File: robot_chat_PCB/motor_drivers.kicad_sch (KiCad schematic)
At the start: 22 parts, among them IC401 NCS199A3RSQT2G, IC402 NCS199A3RSQT2G, J401 Conn_01x06, J402 Conn_01x06, U401 ZXBM5210-SP-13, U402 ZXBM5210-SP-13

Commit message: Mise à jour placement
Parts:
- removed U401, U402: ZXBM5210-SP-13, Package_SO:SOIC-8-1EP_3.9x4.9mm_P1.27mm_EP2.62x3.51mm_ThermalVias, symbol Driver_Motor:ZXBM5210-S
- added U401, U402: ZXBM5210-SP, Package_SO:SOIC-8-1EP_3.9x4.9mm_P1.27mm_EP2.62x3.51mm_ThermalVias, symbol Driver_Motor:ZXBM5210-SP
- C201, C401, C404: footprint Capacitor_SMD:C_0603_1608Metric -> Capacitor_SMD:C_0402_1005Metric
- J401: value Conn_01x06 -> L_Mot
- J402: value Conn_01x06 -> R_Mot
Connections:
- net +3V3: now also U401.3 (VDD), U401.6 (VREF), U402.3 (VDD), U402.6 (VREF)
- net FWD_L: now also U402.4 (FWD)
- net FWD_R: now also U401.4 (FWD)
- net GND: now also U401.8 (GND), U401.9 (GND), U402.8 (GND), U402.9 (GND)
- net MOTOR_L+: now also J401.1 (Pin_1), U402.7 (OUT2); no longer J401.6 (Pin_6)
- net MOTOR_L-: now also J401.6 (Pin_6), U402.1 (OUT1); no longer J401.1 (Pin_1)
- net MOTOR_R+: now also J402.1 (Pin_1), U401.7 (OUT2); no longer J402.6 (Pin_6)
- net MOTOR_R-: now also J402.6 (Pin_6), U401.1 (OUT1); no longer J402.1 (Pin_1)
- net REV_L: now also U402.5 (REV)
- net REV_R: now also U401.5 (REV)
- net RSENSE_L-: now also U402.2 (VM)
- net RSENSE_R-: now also U401.2 (VM)

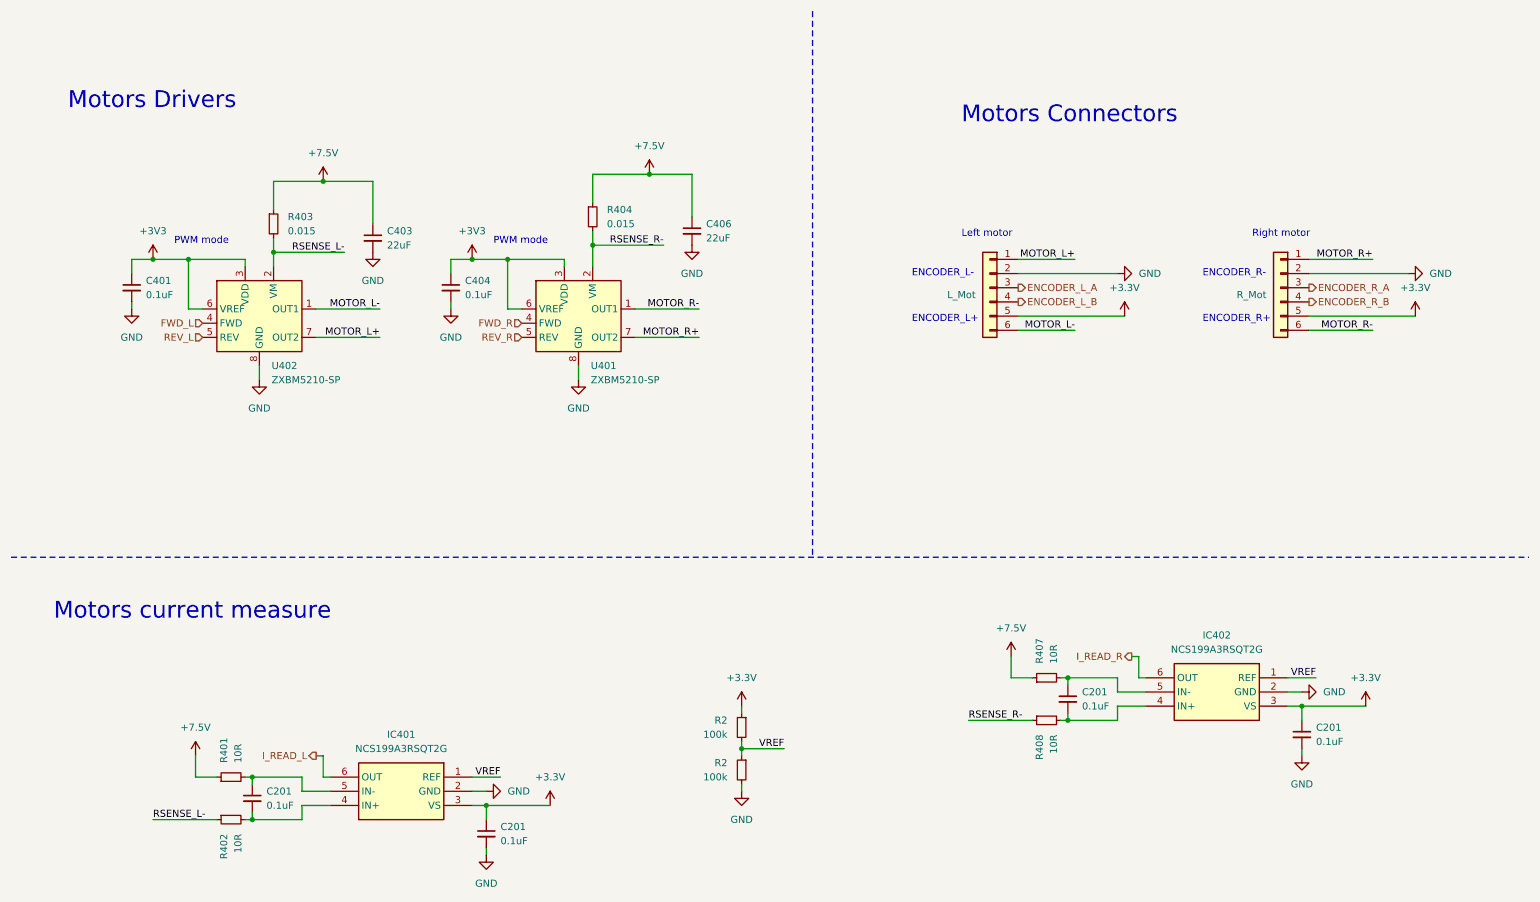
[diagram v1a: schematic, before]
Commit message: changed Rsense position
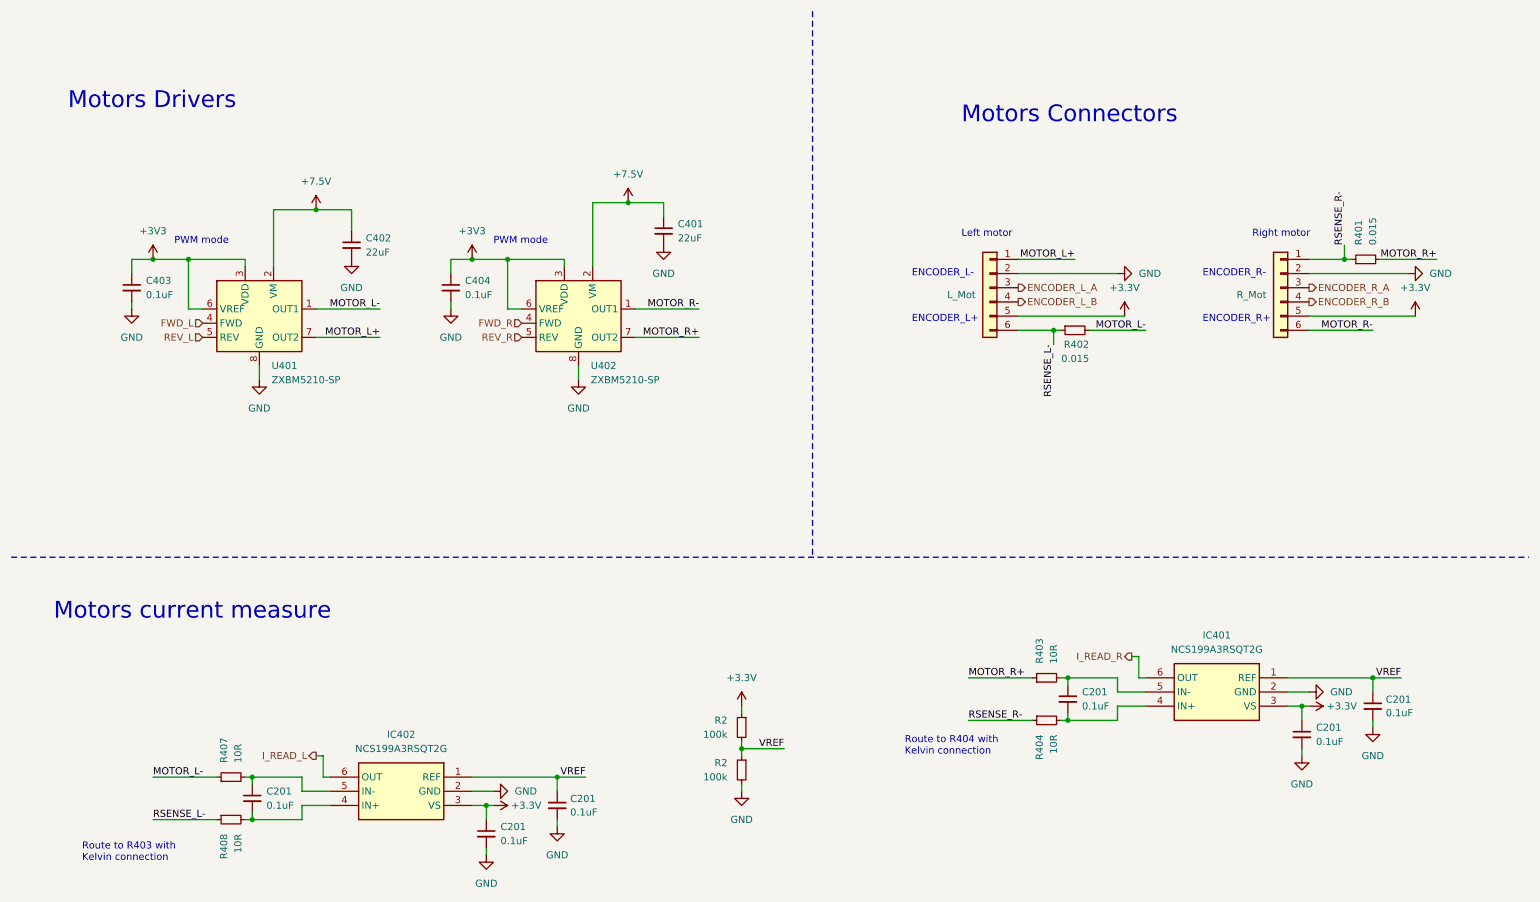
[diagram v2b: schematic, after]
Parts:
- added C201 (x2): 0.1uF, Capacitor_SMD:C_0402_1005Metric, symbol Device:C_Small
- renumbered C406 to C401, C403 to C402, C401 to C403, IC402 to IC401, IC401 to IC402, R404 to R401, R403 to R402, R407 to R403, R408 to R404, R401 to R407, R402 to R408, U402 to U401, U401 to U402
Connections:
- net +7.5V: now also U401.2 (VM), U402.2 (VM); no longer R401.1, R402.1, R403.1, R407.1
- net GND: now also C201.2, C201.2
- net MOTOR_L-: now also R402.2, R407.1; no longer J401.6 (Pin_6)
- net MOTOR_R+: now also R401.2, R403.1; no longer J402.1 (Pin_1)
- net RSENSE_L-: now also J401.6 (Pin_6), R402.1; no longer R402.2, U401.2 (VM)
- net RSENSE_R-: now also J402.1 (Pin_1), R401.1; no longer R401.2, U402.2 (VM)
- net VREF: now also C201.1, C201.1
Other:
- note added: "Route to R403 with Kelvin connection"
- note added: "Route to R404 with Kelvin connection"
- moved on the sheet: C401, C402, R401, R402

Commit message: Routage
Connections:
- net +3V3 is gone; now on net +3.3V: C403.1, C404.1, U401.3 (VDD), U401.6 (VREF), U402.3 (VDD), U402.6 (VREF)
- net MOTOR_L-: now also R408.1; no longer R407.1
- net RSENSE_L-: now also R407.1; no longer R408.1
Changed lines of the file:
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@@
   (junction (at 44.45 57.15) (diameter 0) (color 0 0 0 0)
   )
+  (junction (at 36.83 57.15) (diameter 0) (color 0 0 0 0)
+  )
   (junction (at 55.88 149.86) (diameter 0) (color 0 0 0 0)
   )
+  (junction (at 93.98 57.15) (diameter 0) (color 0 0 0 0)
+  )
   (junction (at 55.88 157.48) (diameter 0) (color 0 0 0 0)
   )
@@
   (junction (at 67.31 48.26) (diameter 0) (color 0 0 0 0)
   )
-  (junction (at 38.1 57.15) (diameter 0) (color 0 0 0 0)
-  )
   (junction (at 199.39 69.85) (diameter 0) (color 0 0 0 0)
   )
   (junction (at 201.93 139.7) (diameter 0) (color 0 0 0 0)
   )
-  (junction (at 95.25 57.15) (diameter 0) (color 0 0 0 0)
-  )
   (junction (at 101.6 57.15) (diameter 0) (color 0 0 0 0)
   )
@@
     (stroke (width 0) (type default))
   )
-  (wire (pts (xy 95.25 57.15) (xy 101.6 57.15))
+  (wire (pts (xy 91.44 57.15) (xy 93.98 57.15))
     (stroke (width 0) (type default))
   )
@@
   )
   (wire (pts (xy 91.44 59.69) (xy 91.44 57.15))
-    (stroke (width 0) (type default))
-  )
-  (wire (pts (xy 91.44 57.15) (xy 95.25 57.15))
     (stroke (width 0) (type default))
   )
@@
     (stroke (width 0) (type default))
   )
+  (wire (pts (xy 93.98 57.15) (xy 101.6 57.15))
+    (stroke (width 0) (type default))
+  )
   (wire (pts (xy 135.89 66.04) (xy 124.46 66.04))
     (stroke (width 0) (type default))
@@
     (stroke (width 0) (type default))
   )
-  (wire (pts (xy 34.29 57.15) (xy 38.1 57.15))
-    (stroke (width 0) (type default))
-  )
   (wire (pts (xy 256.54 69.85) (xy 245.11 69.85))
     (stroke (width 0) (type default))
   )
-  (wire (pts (xy 38.1 57.15) (xy 44.45 57.15))
+  (wire (pts (xy 34.29 57.15) (xy 36.83 57.15))
     (stroke (width 0) (type default))
   )
@@
   )
   (wire (pts (xy 44.45 66.04) (xy 44.45 57.15))
+    (stroke (width 0) (type default))
+  )
+  (wire (pts (xy 36.83 57.15) (xy 44.45 57.15))
     (stroke (width 0) (type default))
   )
@@
     (effects (font (size 1.27 1.27)) (justify right bottom))
   )
-  (label "MOTOR_L-" (at 38.1 149.86 0) (fields_autoplaced)
+  (label "MOTOR_L-" (at 38.1 157.48 0) (fields_autoplaced)
     (effects (font (size 1.27 1.27)) (justify left bottom))
   )
@@
     (effects (font (size 1.27 1.27)) (justify left bottom))
   )
-  (label "RSENSE_L-" (at 38.1 157.48 0) (fields_autoplaced)
+  (label "RSENSE_L-" (at 38.1 149.86 0) (fields_autoplaced)
     (effects (font (size 1.27 1.27)) (justify left bottom))
   )
@@
     )
   )
-  (symbol (lib_id "power:+3V3") (at 95.25 57.15 0) (unit 1)
-    (in_bom yes) (on_board yes) (dnp no) (fields_autoplaced)
-    (property "Reference" "#PWR0406" (at 95.25 60.96 0)
-      (effects (font (size 1.27 1.27)) hide)
-    )
-    (property "Value" "+3V3" (at 95.25 52.07 0)
-      (effects (font (size 1.27 1.27)))
-    )
-    (property "Footprint" "" (at 95.25 57.15 0)
-      (effects (font (size 1.27 1.27)) hide)
-    )
-    (property "Datasheet" "" (at 95.25 57.15 0)
-      (effects (font (size 1.27 1.27)) hide)
-    )
-    (pin "1")
-    (instances
-      (project "robot_chat"
-        (path "/74bedd9b-ffd1-4d8b-87e0-848eab324d95/3a48450b-e017-4419-b5cf-8fa4cfefad60"
-          (reference "#PWR0406") (unit 1)
-        )
-      )
-    )
-  )
   (symbol (lib_id "power:GND") (at 243.84 146.05 0) (unit 1)
     (in_bom yes) (on_board yes) (dnp no) (fields_autoplaced)
@@
         (path "/74bedd9b-ffd1-4d8b-87e0-848eab324d95/3a48450b-e017-4419-b5cf-8fa4cfefad60"
           (reference "C406") (unit 1)
+        )
+      )
+    )
+  )
+  (symbol (lib_id "power:+3.3V") (at 36.83 57.15 0) (unit 1)
+    (in_bom yes) (on_board yes) (dnp no) (fields_autoplaced)
+    (property "Reference" "#PWR0425" (at 36.83 60.96 0)
+      (effects (font (size 1.27 1.27)) hide)
+    )
+    (property "Value" "+3.3V" (at 36.83 52.07 0)
+      (effects (font (size 1.27 1.27)))
+    )
+    (property "Footprint" "" (at 36.83 57.15 0)
+      (effects (font (size 1.27 1.27)) hide)
+    )
+    (property "Datasheet" "" (at 36.83 57.15 0)
+      (effects (font (size 1.27 1.27)) hide)
+    )
+    (pin "1")
+    (instances
+      (project "robot_chat"
+        (path "/74bedd9b-ffd1-4d8b-87e0-848eab324d95/3a48450b-e017-4419-b5cf-8fa4cfefad60"
+          (reference "#PWR0425") (unit 1)
         )
       )
@@
     )
   )
-  (symbol (lib_id "power:+3V3") (at 38.1 57.15 0) (unit 1)
-    (in_bom yes) (on_board yes) (dnp no) (fields_autoplaced)
-    (property "Reference" "#PWR0404" (at 38.1 60.96 0)
-      (effects (font (size 1.27 1.27)) hide)
-    )
-    (property "Value" "+3V3" (at 38.1 52.07 0)
-      (effects (font (size 1.27 1.27)))
-    )
-    (property "Footprint" "" (at 38.1 57.15 0)
-      (effects (font (size 1.27 1.27)) hide)
-    )
-    (property "Datasheet" "" (at 38.1 57.15 0)
-      (effects (font (size 1.27 1.27)) hide)
-    )
-    (pin "1")
-    (instances
-      (project "robot_chat"
-        (path "/74bedd9b-ffd1-4d8b-87e0-848eab324d95/3a48450b-e017-4419-b5cf-8fa4cfefad60"
-          (reference "#PWR0404") (unit 1)
-        )
-      )
-    )
-  )
   (symbol (lib_id "Device:C_Small") (at 110.49 154.94 0) (unit 1)
     (in_bom yes) (on_board yes) (dnp no) (fields_autoplaced)
@@
         )
       )
+    )
+  )
+  (symbol (lib_id "power:+3.3V") (at 93.98 57.15 0) (unit 1)
+    (in_bom yes) (on_board yes) (dnp no) (fields_autoplaced)
+    (property "Reference" "#PWR0404" (at 93.98 60.96 0)
+      (effects (font (size 1.27 1.27)) hide)
+    )
+    (property "Value" "+3.3V" (at 93.98 52.07 0)
+      (effects (font (size 1.27 1.27)))
+    )
+    (property "Footprint" "" (at 93.98 57.15 0)
+      (effects (font (size 1.27 1.27)) hide)
+    )
+    (property "Datasheet" "" (at 93.98 57.15 0)
+      (effects (font (size 1.27 1.27)) hide)
+    )
+    (pin "1")
+    (instances
+      (project "robot_chat"
+        (path "/74bedd9b-ffd1-4d8b-87e0-848eab324d95/3a48450b-e017-4419-b5cf-8fa4cfefad60"
+          (reference "#PWR0404") (unit 1)
+        )
+      )

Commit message: Routage final v1.2
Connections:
- net IN_R+: now reaches C201.2, IC401.4 (IN+), R404.2
- net IN_R-: now reaches C201.1, IC401.5 (IN-), R403.2
- net IN_L-: now reaches C201.1, IC402.5 (IN-), R407.2
- net IN_L+: now reaches C201.2, IC402.4 (IN+), R408.2
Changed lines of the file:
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@@
     (stroke (width 0) (type default))
   )
-  (wire (pts (xy 210.82 132.08) (xy 201.93 132.08))
+  (wire (pts (xy 208.28 132.08) (xy 201.93 132.08))
     (stroke (width 0) (type default))
   )
@@
     (stroke (width 0) (type default))
   )
-  (wire (pts (xy 55.88 157.48) (xy 64.77 157.48))
+  (wire (pts (xy 55.88 157.48) (xy 62.23 157.48))
     (stroke (width 0) (type default))
   )
@@
     (stroke (width 0) (type default))
   )
-  (wire (pts (xy 201.93 139.7) (xy 210.82 139.7))
+  (wire (pts (xy 201.93 139.7) (xy 208.28 139.7))
     (stroke (width 0) (type default))
   )
@@
     (stroke (width 0) (type default))
   )
-  (wire (pts (xy 64.77 157.48) (xy 64.77 154.94))
+  (wire (pts (xy 62.23 157.48) (xy 62.23 154.94))
     (stroke (width 0) (type default))
   )
@@
     (stroke (width 0) (type default))
   )
-  (wire (pts (xy 210.82 139.7) (xy 210.82 137.16))
+  (wire (pts (xy 208.28 139.7) (xy 208.28 137.16))
     (stroke (width 0) (type default))
   )
@@
     (stroke (width 0) (type default))
   )
-  (wire (pts (xy 215.9 134.62) (xy 210.82 134.62))
-    (stroke (width 0) (type default))
-  )
-  (wire (pts (xy 210.82 137.16) (xy 215.9 137.16))
+  (wire (pts (xy 215.9 134.62) (xy 208.28 134.62))
+    (stroke (width 0) (type default))
+  )
+  (wire (pts (xy 208.28 137.16) (xy 215.9 137.16))
     (stroke (width 0) (type default))
   )
@@
     (stroke (width 0) (type default))
   )
-  (wire (pts (xy 69.85 152.4) (xy 64.77 152.4))
+  (wire (pts (xy 69.85 152.4) (xy 62.23 152.4))
     (stroke (width 0) (type default))
   )
@@
     (stroke (width 0) (type default))
   )
-  (wire (pts (xy 64.77 149.86) (xy 55.88 149.86))
+  (wire (pts (xy 62.23 149.86) (xy 55.88 149.86))
     (stroke (width 0) (type default))
   )
@@
     (stroke (width 0) (type dash))
   )
-  (wire (pts (xy 64.77 154.94) (xy 69.85 154.94))
-    (stroke (width 0) (type default))
-  )
-  (wire (pts (xy 210.82 134.62) (xy 210.82 132.08))
-    (stroke (width 0) (type default))
-  )
-  (wire (pts (xy 64.77 152.4) (xy 64.77 149.86))
+  (wire (pts (xy 62.23 154.94) (xy 69.85 154.94))
+    (stroke (width 0) (type default))
+  )
+  (wire (pts (xy 208.28 134.62) (xy 208.28 132.08))
+    (stroke (width 0) (type default))
+  )
+  (wire (pts (xy 62.23 152.4) (xy 62.23 149.86))
     (stroke (width 0) (type default))
   )
@@
     (effects (font (size 1.27 1.27)) (justify right bottom))
   )
+  (label "IN_R-" (at 215.9 134.62 180) (fields_autoplaced)
+    (effects (font (size 1.27 1.27)) (justify right bottom))
+  )
   (label "MOTOR_L+" (at 203.2 57.15 180) (fields_autoplaced)
     (effects (font (size 1.27 1.27)) (justify right bottom))
   )
+  (label "IN_L-" (at 69.85 152.4 180) (fields_autoplaced)
+    (effects (font (size 1.27 1.27)) (justify right bottom))
+  )
+  (label "IN_L+" (at 69.85 154.94 180) (fields_autoplaced)
+    (effects (font (size 1.27 1.27)) (justify right bottom))
+  )
   (label "MOTOR_L-" (at 215.9 69.85 180) (fields_autoplaced)
     (effects (font (size 1.27 1.27)) (justify right bottom))
@@
   )
   (label "MOTOR_R-" (at 256.54 69.85 180) (fields_autoplaced)
+    (effects (font (size 1.27 1.27)) (justify right bottom))
+  )
+  (label "IN_R+" (at 215.9 137.16 180) (fields_autoplaced)
     (effects (font (size 1.27 1.27)) (justify right bottom))
   )
@@
   )
   (symbol (lib_id "Device:C_Small") (at 201.93 135.89 0) (unit 1)
-    (in_bom yes) (on_board yes) (dnp no) (fields_autoplaced)
-    (property "Reference" "C201" (at 204.47 134.6263 0)
-      (effects (font (size 1.27 1.27)) (justify left))
-    )
-    (property "Value" "0.1uF" (at 204.47 137.1663 0)
+    (in_bom yes) (on_board yes) (dnp no)
+    (property "Reference" "C201" (at 194.31 134.62 0)
+      (effects (font (size 1.27 1.27)) (justify left))
+    )
+    (property "Value" "0.1uF" (at 194.31 137.16 0)
       (effects (font (size 1.27 1.27)) (justify left))
     )
@@
   )
   (symbol (lib_id "Device:C_Small") (at 55.88 153.67 0) (unit 1)
-    (in_bom yes) (on_board yes) (dnp no) (fields_autoplaced)
-    (property "Reference" "C201" (at 58.42 152.4063 0)
-      (effects (font (size 1.27 1.27)) (justify left))
-    )
-    (property "Value" "0.1uF" (at 58.42 154.9463 0)
-      (effects (font (size 1.27 1.27)) (justify left))
-    )
+    (in_bom yes) (on_board yes) (dnp no)
+    (property "Reference" "C201" (at 48.26 152.4 0)
+      (effects (font (size 1.27 1.27)) (justify left))
+    )
+    (property "Value" "0.1uF" (at 48.26 154.94 0)
+      (effects (font (size 1.27 1.27)) (justify left))
+    )

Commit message: fixed DRC, added html bom
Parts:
- IC401, IC402: Farnell Part Number (none) -> 2981170
- J401, J402: Farnell Part Number (none) -> 1516294
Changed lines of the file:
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@@
+      (effects (font (size 1.27 1.27)) hide)
+    )
+    (property "Farnell Part Number" "1516294" (at 240.03 62.23 0)
       (effects (font (size 1.27 1.27)) hide)
     )
@@
       (effects (font (size 1.27 1.27)) hide)
     )
+    (property "Farnell Part Number" "1516294" (at 187.96 62.23 0)
+      (effects (font (size 1.27 1.27)) hide)
+    )
     (pin "1")
     (pin "2")
@@
     (property "Manufacturer_Part_Number" "NCS199A3RSQT2G" (at 219.71 927 0)
       (effects (font (size 1.27 1.27)) (justify left top) hide)
+    )
+    (property "Farnell Part Number" "2981170" (at 241.3 132.08 0)
+      (effects (font (size 1.27 1.27)) hide)
     )
     (pin "1")
@@
       (effects (font (size 1.27 1.27)) (justify left top) hide)
     )
-    (pin "1")
+    (property "Farnell Part Number" "2981170" (at 95.25 149.86 0)
+      (effects (font (size 1.27 1.27)) hide)
+    )
+    (pin "1")
